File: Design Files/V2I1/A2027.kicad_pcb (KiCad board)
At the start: 2 copper layers, 78 parts, among them J1 Screw_Terminal_01x02, J3 Conn_02x03_Top_Bottom, J4 Conn_01x05_Pin, J6 Conn_01x02_Pin, J7 Conn_01x04_Pin, Q1 BSS138, Q2 BC857, Q3 BSS138, Q4 BC857, SW1 SW_SPDT, U1 TPS560200, U2 USBLC6-2SC6, U4 STM32F103C8T6, U5 LM1117MP-3.3, U6 DS3232M, U8 24LC256, Y1 16MHz

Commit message: master :: update schmea
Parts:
- added BT1: 3.0V, Battery:BatteryHolder_Keystone_3034_1x20mm, F.Cu at (117.4, 89.0)
- added U3: TPS2113A, Package_SO:TSSOP-8_4.4x3mm_P0.65mm, F.Cu at (130.2, 121.9)
- added U7: MAX3232, Package_SO:TSSOP-16_4.4x5mm_P0.65mm, F.Cu at (151.8, 113.7)
- SW1: footprint Button_Switch_THT:SW_E-Switch_EG1224_SPDT_Angled -> Button_Switch_SMD:SW_SPDT_PCM12
- moved J4 70.9 mm to (145.3, 80.3)
- moved SW1 69.0 mm to (142.1, 113.4)
- moved D10 57.3 mm to (132.0, 94.2)
- moved D11 57.3 mm to (132.0, 97.2)
- moved D3 57.3 mm to (132.0, 79.5)
- moved D4 57.3 mm to (132.0, 82.4)
- moved D5 57.3 mm to (132.0, 85.4)
- moved D8 57.3 mm to (132.0, 88.3)
- moved D9 57.3 mm to (132.0, 91.3)
- moved C18 57.1 mm to (141.0, 89.3)
- moved C2 57.1 mm to (141.0, 79.3)
- moved C4 57.1 mm to (141.0, 81.8)
- moved C7 57.1 mm to (141.0, 86.8)
- moved C5 57.1 mm to (141.0, 84.3)
- moved FB1 57.1 mm to (141.0, 91.8)
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
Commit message: placement
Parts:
- removed J7: Conn_01x04_Pin, Connector_PinHeader_2.54mm:PinHeader_1x04_P2.54mm_Vertical
- added D12: D_TVS, Diode_SMD:D_SOD-323, F.Cu at (248.2, 91.5)
- added J2: USB_B_Micro, Connector_USB:USB_Micro-B_Wuerth_629105150521, F.Cu at (225.0, 44.9)
- added J5: Conn_01x04_Pin, Connector_PinHeader_2.54mm:PinHeader_1x04_P2.54mm_Vertical, F.Cu at (260.6, 95.7)
- added JP1: SolderJumper_3_Open, Jumper:SolderJumper-3_P2.0mm_Open_TrianglePad1.0x1.5mm, F.Cu at (236.8, 95.2)
- added R20: 1k5, Resistor_SMD:R_0402_1005Metric, F.Cu at (21.5, 49.5)
- BT1: moved to B.Cu
- D1: value RED -> SS14; footprint LED_SMD:LED_0603_1608Metric -> Diode_SMD:D_SMA
- D3: value D_TVS -> RED; footprint Diode_SMD:D_SOD-323 -> LED_SMD:LED_0603_1608Metric
- D6: value YELLOW -> D_TVS; footprint LED_SMD:LED_0603_1608Metric -> Diode_SMD:D_SOD-323
- D8: value D_TVS -> YELLOW; footprint Diode_SMD:D_SOD-323 -> LED_SMD:LED_0603_1608Metric
- J3: value Conn_02x03_Top_Bottom -> Conn_01x05_Pin; footprint Connector_PinHeader_2.54mm:PinHeader_2x03_P2.54mm_Vertical -> Connector_PinHeader_2.54mm:PinHeader_1x05_P2.54mm_Vertical
- J4: value Conn_01x05_Pin -> DE9_Pins; footprint Connector_PinHeader_2.54mm:PinHeader_1x05_P2.54mm_Vertical -> Connector_Dsub:DSUB-9_Pins_Horizontal_P2.77x2.84mm_EdgePinOffset7.70mm_Housed_MountingHolesOffset9.12mm
- J6: value Conn_01x02_Pin -> Conn_01x04_Pin; footprint Connector_PinHeader_2.54mm:PinHeader_1x02_P2.54mm_Vertical -> Connector_PinHeader_2.54mm:PinHeader_1x04_P2.54mm_Vertical
- R10: value 700R -> 10k
- R11: value 1k5 -> 700R
- R12: value 4k7 -> 1k5
- R15, R17: value 10k -> 4k7
- R16: value 4k7 -> 10k
- R18: value 1k5 -> 10k
- R8: value 47k -> 10k
- R9: value 10k -> 47k
- moved C28 152.3 mm to (257.7, 66.0), turned to 90 degrees
- moved C25 146.0 mm to (254.2, 71.0)
- moved R13 145.5 mm to (21.5, 24.5), turned to -90 degrees
- moved C23 144.8 mm to (251.4, 61.2), turned to 180 degrees
- moved C27 144.8 mm to (250.4, 66.0), turned to 90 degrees
- moved C10 143.8 mm to (245.5, 72.4), turned to -90 degrees
- moved C24 143.4 mm to (252.0, 71.0)
- moved R14 143.1 mm to (26.2, 22.5), turned to -90 degrees
- moved R17 143.0 mm to (21.5, 31.2), turned to -90 degrees
- moved R19 141.3 mm to (21.3, 41.0), turned to 180 degrees
- moved C11 138.6 mm to (241.8, 80.9), turned to 180 degrees
- moved C15 137.9 mm to (245.0, 80.2), turned to -90 degrees
- moved R15 137.7 mm to (26.5, 29.2), turned to -90 degrees
- moved J3 136.1 mm to (268.2, 75.5)
- moved C29 135.9 mm to (247.8, 103.4), turned to -90 degrees
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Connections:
- D1 pad 1: /5V_LED_K -> +12V
- D1 pad 2: +5V_EXT -> Net-(D1-A)
- D10 pad 2: /H_I2C_SDA -> /I2C2_SCL
- D11 pad 2: /H_I2C_SCL -> /H_I2C_SDA
- D2 pad 1: /3V3_LED_K -> /5V_LED_K
- D2 pad 2: +3.3V -> +5V_EXT
- D3 pad 1: GND -> /3V3_LED_K
- D3 pad 2: /SWDIO -> +3.3V
- D4 pad 2: /SWCLK -> /SWDIO
- D5 pad 2: /NRST -> /SWCLK
- D6 pad 1: Net-(D6-K) -> GND
- D6 pad 2: Net-(D6-A) -> /NRST
- D8 pad 1: GND -> Net-(D8-K)
- D8 pad 2: /I2C2_SDA -> Net-(D8-A)
- D9 pad 2: /I2C2_SCL -> /I2C2_SDA
- J1 pad 1: +12V -> Net-(D1-A)
- J3 pad 1: Net-(J3-Pin_1) -> +3.3V
- J3 pad 2: Net-(J3-Pin_2) -> /SWDIO
- J3 pad 3: Net-(J3-Pin_3) -> /SWCLK
- J3 pad 4: Net-(J3-Pin_4) -> /NRST
- J3 pad 5: Net-(J3-Pin_5) -> GND
- J4 pad 1: +3.3V -> unconnected-(J4-Pad1)
- J4 pad 2: /SWDIO -> /DB9_RX
- J4 pad 3: /SWCLK -> /DB9_TX
- J4 pad 4: /NRST -> unconnected-(J4-Pad4)
- J6 pad 1: /I2C2_SCL -> +5V_SYS
- J6 pad 2: /I2C2_SDA -> /H_I2C_SCL
- Q2 pad 3: Net-(D6-A) -> Net-(D7-A)
- Q4 pad 3: Net-(D7-A) -> Net-(D8-A)
- R10 pad 2: Net-(U3-ILIM) -> Net-(U3-VSNS)
- R11 pad 1: /3V3_LED_K -> GND
- R11 pad 2: GND -> Net-(U3-ILIM)
- R12 pad 1: +3.3V -> /3V3_LED_K
- R12 pad 2: /I2C2_SCL -> GND
- R13 pad 1: +5V_SYS -> +3.3V
- R13 pad 2: /H_I2C_SCL -> /I2C2_SCL
- R14 pad 2: /H_I2C_SDA -> /H_I2C_SCL
- R15 pad 1: /USART1_TX -> +5V_SYS
- R15 pad 2: Net-(Q2-B) -> /H_I2C_SDA
- R16 pad 1: +3.3V -> /USART1_TX
- R16 pad 2: /I2C2_SDA -> Net-(Q2-B)
- R17 pad 1: /USART1_RX -> +3.3V
- R17 pad 2: Net-(Q4-B) -> /I2C2_SDA
- R18 pad 1: Net-(D6-K) -> /USART1_RX
- R18 pad 2: GND -> Net-(Q4-B)
- R3 pad 2: Net-(U1-FB) -> GND
- R8 pad 1: /USB_VBUS_SENSE -> Net-(JP1-C)
- R8 pad 2: GND -> Net-(U4-PB2)
- R9 pad 1: GND -> /USB_VBUS_SENSE
- R9 pad 2: Net-(U3-VSNS) -> GND
- U2 pad 1: /USB_D+ -> /E_USB_D-
- U2 pad 3: /USB_D- -> /E_USB_D+
- U2 pad 4: /E_USB_D- -> /USB_D+
- U2 pad 6: /E_USB_D+ -> /USB_D-
- U4 pad 12: /EEPROM_WP -> unconnected-(U4-PA2-Pad12)
- U4 pad 18: Net-(J3-Pin_4) -> unconnected-(U4-PB0-Pad18)
- U4 pad 19: Net-(J3-Pin_5) -> unconnected-(U4-PB1-Pad19)
- U4 pad 2: Net-(J3-Pin_1) -> unconnected-(U4-PC13-Pad2)
- U4 pad 20: Net-(J3-Pin_6) -> Net-(U4-PB2)
- U4 pad 3: Net-(J3-Pin_2) -> unconnected-(U4-PC14-Pad3)
- U4 pad 4: Net-(J3-Pin_3) -> unconnected-(U4-PC15-Pad4)
- U8 pad 7: /EEPROM_WP -> unconnected-(U8-WP-Pad7)

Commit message: master :: board outline
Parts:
- added H1: MountingHole, MountingHole:MountingHole_3.2mm_M3, F.Cu at (181.8, 74.5)
- added H2: MountingHole_Pad, MountingHole:MountingHole_3.2mm_M3_Pad_TopBottom, F.Cu at (181.8, 134.5)
- added H3: MountingHole_Pad, MountingHole:MountingHole_3.2mm_M3_Pad_TopBottom, F.Cu at (101.8, 134.5)
- added H4: MountingHole_Pad, MountingHole:MountingHole_3.2mm_M3_Pad_TopBottom, F.Cu at (101.8, 74.5)
- BT1: moved to F.Cu
- moved R19 167.5 mm to (175.7, 105.8), turned to 0 degrees
- moved R15 165.5 mm to (164.9, 120.0), turned to 180 degrees
- moved D7 165.3 mm to (175.2, 104.0), turned to 180 degrees
- moved R14 165.1 mm to (159.5, 120.0), turned to 180 degrees
- moved R17 164.6 mm to (163.0, 115.2), turned to 180 degrees
- moved Q3 163.6 mm to (163.0, 118.2), turned to -90 degrees
- moved R13 163.5 mm to (157.5, 115.2), turned to 180 degrees
- moved Q1 162.7 mm to (157.5, 118.2), turned to -90 degrees
- moved R20 161.7 mm to (175.5, 98.8), turned to 0 degrees
- moved Q2 161.5 mm to (172.5, 105.8), turned to 0 degrees
- moved D8 159.8 mm to (175.0, 97.2), turned to 180 degrees
- moved Q4 155.5 mm to (172.2, 98.8), turned to 0 degrees
- moved R16 154.4 mm to (169.0, 104.8), turned to 0 degrees
- moved R18 148.2 mm to (168.8, 97.8), turned to 0 degrees
- moved SW1 147.4 mm to (99.6, 115.3), turned to -90 degrees
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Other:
- board outline added: 89 x 69 mm

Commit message: master :: routing
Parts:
- R6: footprint Resistor_SMD:R_0402_1005Metric -> Resistor_SMD:R_0603_1608Metric
- moved J3 53.0 mm to (130.7, 117.1), turned to 180 degrees
- moved D5 50.4 mm to (127.7, 111.8), turned to 90 degrees
- moved D4 50.1 mm to (127.7, 117.1), turned to 90 degrees
- moved D6 46.3 mm to (133.5, 106.4), turned to -90 degrees
- moved D8 31.7 mm to (145.7, 85.1), turned to 0 degrees
- moved R20 28.7 mm to (150.0, 85.5)
- moved D7 27.1 mm to (149.2, 96.5), turned to 0 degrees
- moved Q4 26.7 mm to (148.2, 87.2), turned to 90 degrees
- moved R19 24.4 mm to (153.3, 96.1)
- moved Q2 23.7 mm to (151.6, 94.5), turned to -90 degrees
- moved JP1 23.5 mm to (154.4, 108.9), turned to 90 degrees
- moved R16 22.4 mm to (151.1, 91.3), turned to -45 degrees
- moved U8 22.1 mm to (156.6, 101.6), turned to 180 degrees
- moved R18 21.5 mm to (148.5, 90.5), turned to 135 degrees
- moved R8 21.5 mm to (152.4, 107.7), turned to 90 degrees
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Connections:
- U2 pad 1: /E_USB_D- -> /USB_D+
- U2 pad 3: /E_USB_D+ -> /USB_D-
- U2 pad 4: /USB_D+ -> /E_USB_D-
- U2 pad 6: /USB_D- -> /E_USB_D+
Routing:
- net /I2C2_SDA: track 0.00 -> 86.4 mm, vias 0 -> 4
- net /I2C2_SCL: track 0.00 -> 83.2 mm, vias 0 -> 4
- net /BOOT0: track 0.00 -> 41.1 mm, vias 0 -> 2
- net /SWDIO: track 0.00 -> 36.4 mm
- net GND: track 0.00 -> 31.4 mm, vias 0 -> 13
- net /USART1_RX: track 0.00 -> 30.2 mm, vias 0 -> 2
- net /USART1_TX: track 0.00 -> 29.3 mm, vias 0 -> 2
- net /SWCLK: track 0.00 -> 23.9 mm
- net /USB_D-: track 0.00 -> 21.0 mm
- net /USB_D+: track 0.00 -> 21.0 mm
- net /USB_VBUS_SENSE: track 0.00 -> 18.7 mm
- net /NRST: track 0.00 -> 16.3 mm
- net +3.3V: track 0.00 -> 14.0 mm
- net VBUS: track 0.00 -> 10.2 mm, vias 0 -> 2
- net /H_I2C_SDA: track 0.00 -> 9.95 mm
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- added copper zone on B.Cu, net GND

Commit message: master :: 3v3, 5v
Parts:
- moved BT1 63.5 mm to (174.8, 100.6), turned to 90 degrees
- moved C26 30.1 mm to (160.2, 117.8), turned to 180 degrees
- moved U6 28.4 mm to (161.4, 113.1), turned to 90 degrees
- moved D6 26.9 mm to (136.5, 133.1), turned to 180 degrees
- moved R17 26.0 mm to (160.7, 124.8), turned to 180 degrees
- moved R13 23.0 mm to (155.0, 124.9), turned to 180 degrees
- moved D5 21.7 mm to (132.1, 133.1), turned to 180 degrees
- moved R3 20.9 mm to (122.9, 90.6), turned to -90 degrees
- moved D2 20.1 mm to (121.1, 90.6), turned to -90 degrees
- moved J3 19.7 mm to (125.9, 136.2), turned to 90 degrees
- moved D4 15.9 mm to (127.5, 133.0), turned to 0 degrees
- moved C21 11.3 mm to (119.0, 99.9)
- moved C22 10.8 mm to (111.3, 106.1), turned to 0 degrees
- moved U5 7.44 mm to (113.1, 101.1), turned to 180 degrees
- moved R10 6.83 mm to (127.6, 95.5), turned to -90 degrees
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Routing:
- net +5V_EXT: track 0.00 -> 28.3 mm
- net GND: track 31.4 -> 54.0 mm, vias 13 -> 32
- net /NRST: track 16.3 -> 38.0 mm
- net VBUS: track 10.2 -> 29.2 mm
- net /SWCLK: track 23.9 -> 42.6 mm
- net +3.0V_BAT: track 0.00 -> 16.4 mm
- net /I2C2_SCL: track 83.2 -> 67.1 mm, vias 4 -> 2
- net +12V: track 0.00 -> 15.6 mm
- net /I2C2_SDA: track 86.4 -> 70.9 mm, vias 4 -> 0
- net /SWDIO: track 36.4 -> 50.3 mm
- net +5V_SYS: track 0.00 -> 9.70 mm, vias 0 -> 5
- net Net-(D1-A): track 0.00 -> 8.38 mm
- net Net-(U3-VSNS): track 0.00 -> 7.45 mm
- net +3.3V: track 14.0 -> 20.7 mm
- net Net-(U1-FB): track 0.00 -> 6.09 mm
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- added copper zone on F.Cu, net +3.3V
- added copper zone on F.Cu, net +5V_EXT
- added copper zone on B.Cu, net +5V_SYS
- added copper zone on F.Cu, net +5V_SYS

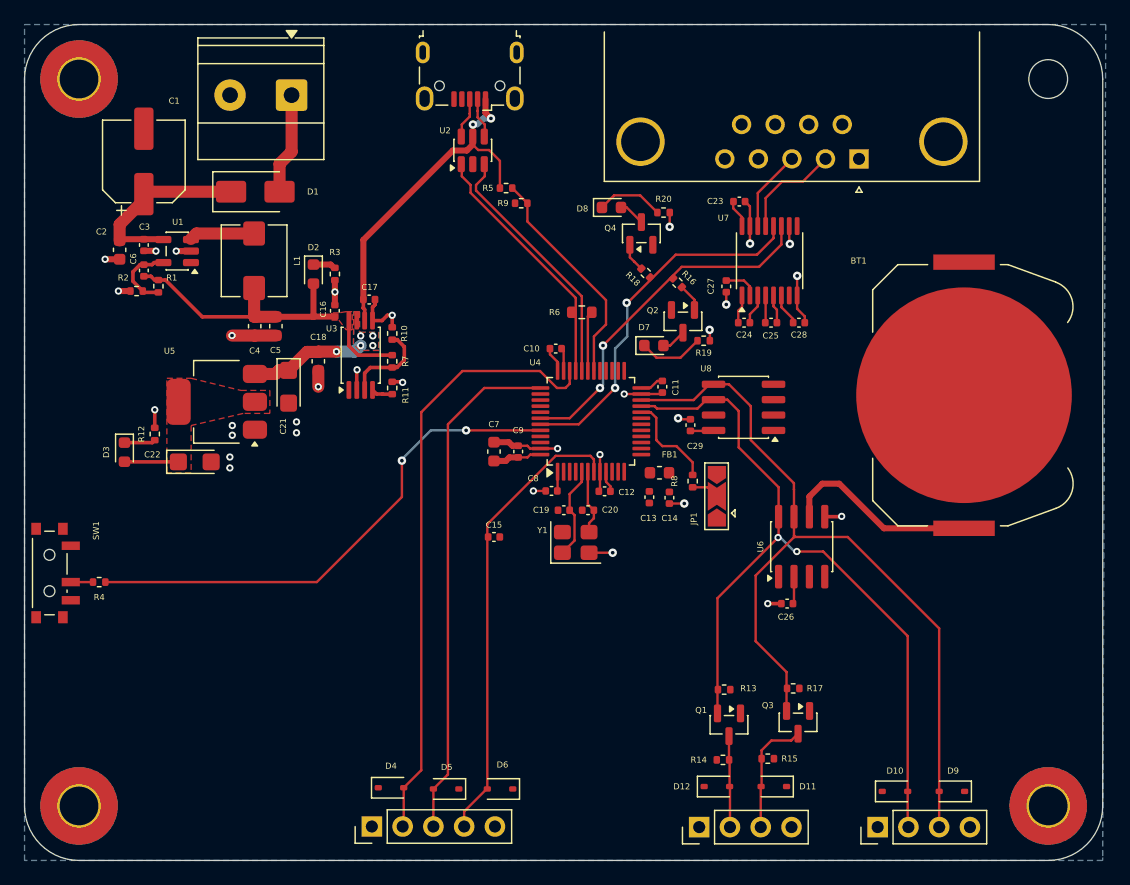
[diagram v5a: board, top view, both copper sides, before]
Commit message: master :: routeing 3v3 5v
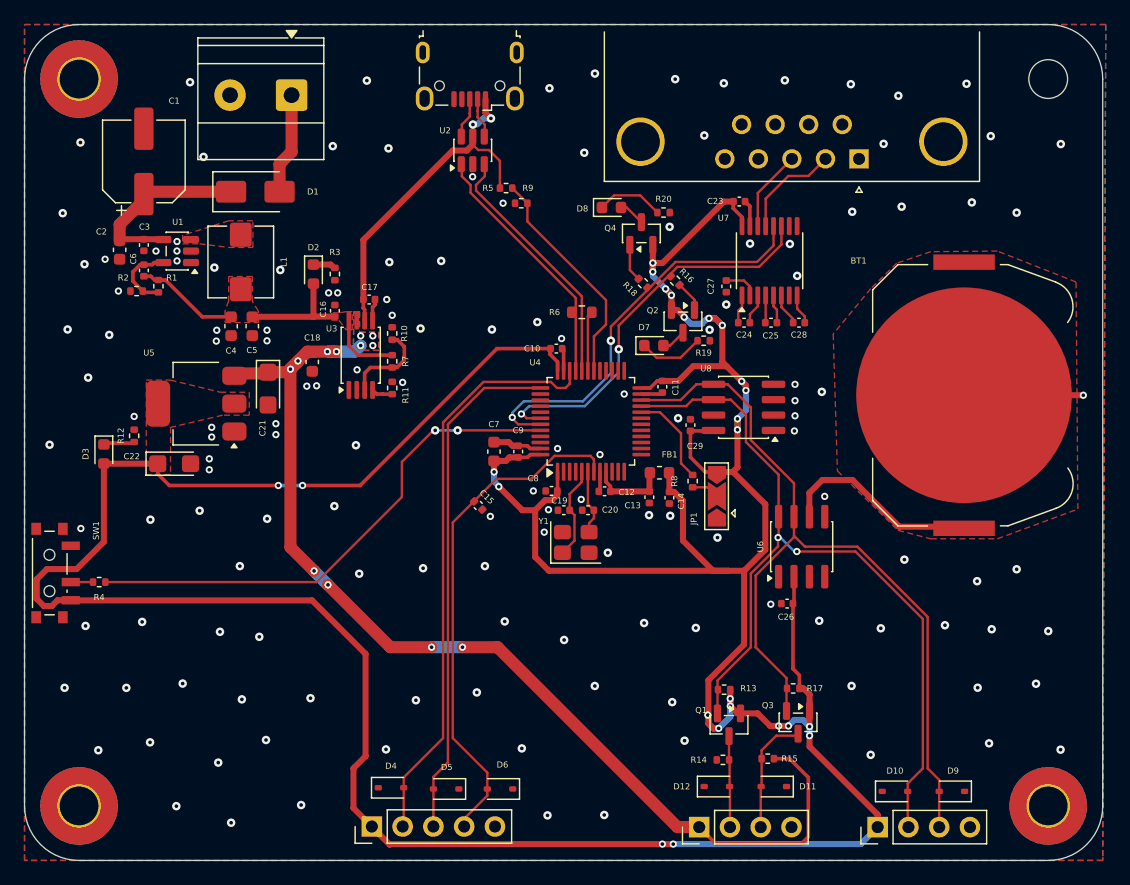
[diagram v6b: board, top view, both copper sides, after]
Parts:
- moved C15 2.91 mm to (134.7, 109.7), turned to -45 degrees
- moved C4 1.95 mm to (114.3, 94.9)
- moved C5 1.95 mm to (116.0, 94.9)
- moved C22 1.71 mm to (109.6, 106.2)
- moved D3 1.71 mm to (103.8, 105.5)
- moved R12 1.71 mm to (106.3, 104.0)
- moved U5 1.71 mm to (111.4, 101.3)
- moved C21 1.71 mm to (117.3, 100.0)
- moved L1 1.10 mm to (115.1, 89.6)
- moved R18 0.87 mm to (148.3, 91.3)
- moved C18 0.50 mm to (121.0, 97.8)
- moved R16 0.26 mm to (151.0, 91.1)
- moved C10 0.05 mm to (141.2, 96.8)
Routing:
- net +3.3V: track 20.7 -> 314.6 mm, vias 0 -> 25
- net +5V_SYS: track 9.70 -> 89.4 mm, vias 5 -> 12
- net GND: track 54.0 -> 26.3 mm, vias 32 -> 144
- net Net-(U1-PH): track 5.40 -> 0.57 mm
- net +3.3VA: track 1.77 -> 6.54 mm
- net +5V_EXT: track 28.3 -> 24.1 mm
- net /NRST: track 38.0 -> 42.1 mm
- net /USART1_RX: track 30.2 -> 34.1 mm
- net /USART1_TX: track 29.3 -> 32.8 mm
- net /I2C2_SCL: track 67.1 -> 69.7 mm
- net /SWDIO: track 50.3 -> 48.0 mm
- net Net-(Q4-B): track 2.37 -> 3.11 mm
- added copper zone on F.Cu, net +3.0V_BAT
- added copper zone on F.Cu, net GND
- added copper zone on F.Cu, net Net-(U1-PH)
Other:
- board text added: "{ "ViaStitcher": "0.3.1", "stitch_zone_0": { "HSpacing": "5", "VSpacing": "5", "HOffset": "0", "VOffset": "0", "Clearance": "0.5", "Randomize": true, "Stagger": true, "OnlyFilledCopper": true } }"
- board text added: "{ "ViaStitcher": "0.3.1", "stitch_zone_0": { "HSpacing": "7", "VSpacing": "7", "HOffset": "0", "VOffset": "3", "Clearance": "1", "Randomize": true, "Stagger": false, "OnlyFilledCopper": true } }"

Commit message: master :: via
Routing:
- net +5V_SYS: track 89.4 -> 97.3 mm, vias 12 -> 10
- net GND: track 26.3 -> 31.5 mm, vias 144 -> 126
- net +3.3V: track 314.6 -> 315.2 mm
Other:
- board text added: "{ "ViaStitcher": "0.3.1", "stitch_zone_0": { "HSpacing": "5", "VSpacing": "5", "HOffset": "0", "VOffset": "3", "Clearance": "1", "FillStyle": "Stagger", "RequireAllCopperLayers": true, "AdaptiveFill": false, "MinSpacingPercent": "80", "MaxSpacingPercent": "150" } }"
- board text removed: "{ "ViaStitcher": "0.3.1", "stitch_zone_0": { "HSpacing": "7", "VSpacing": "7", "HOffset": "0", "VOffset": "3", "Clearance": "1", "Randomize": true, "Stagger": false, "OnlyFilledCopper": true } }"

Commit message: master :: update
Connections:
- net Net-(JP1-C) renamed /SW_BOOT1
- net Net-(U4-PB2) renamed /BOOT1
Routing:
- net GND: vias 126 -> 131
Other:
- board text added: "12V"
- board text added: "2026-10-29 03:08 PM"
- board text added: "A2027 / Rev 0.2"
- board text added: "Author: AD"
- board text added: "BOOT0"
- board text added: "I2C"
- board text added: "I2C_5V"
- board text added: "SWD"
- board text added: "USB"
- board text added: "→ 1"
